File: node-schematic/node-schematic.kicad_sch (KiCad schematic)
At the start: 23 parts, among them U1 NRF52840-QFAA-R7, X1 NX2016SA-32MHZ, X2 32.768kHz

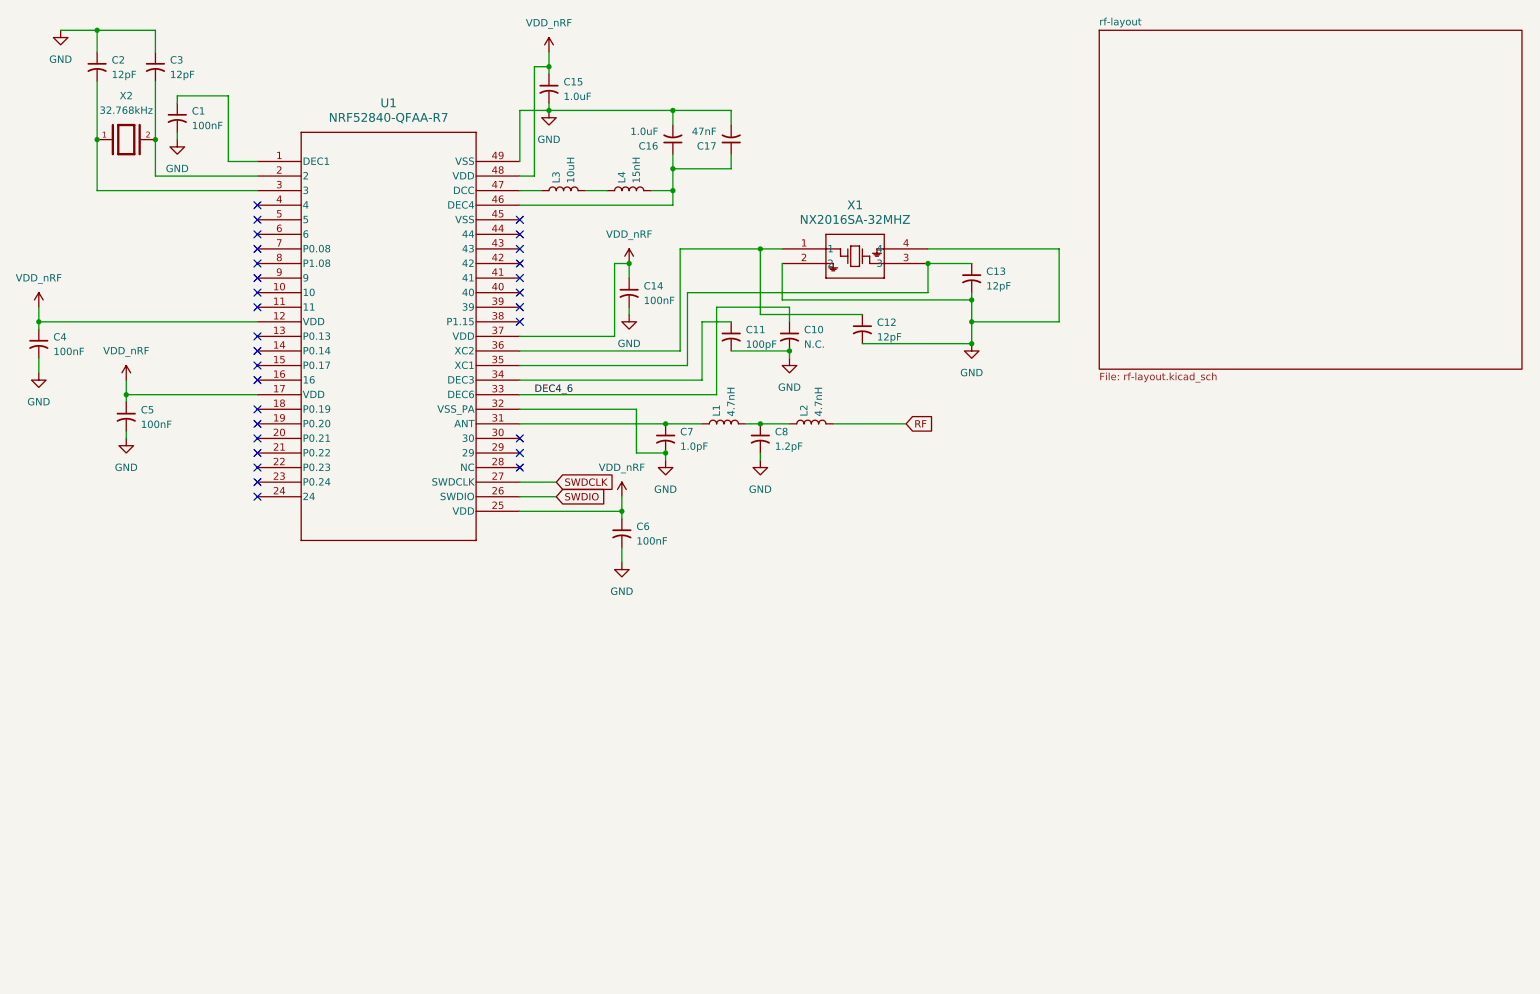
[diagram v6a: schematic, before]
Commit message: fuel gauge implemented
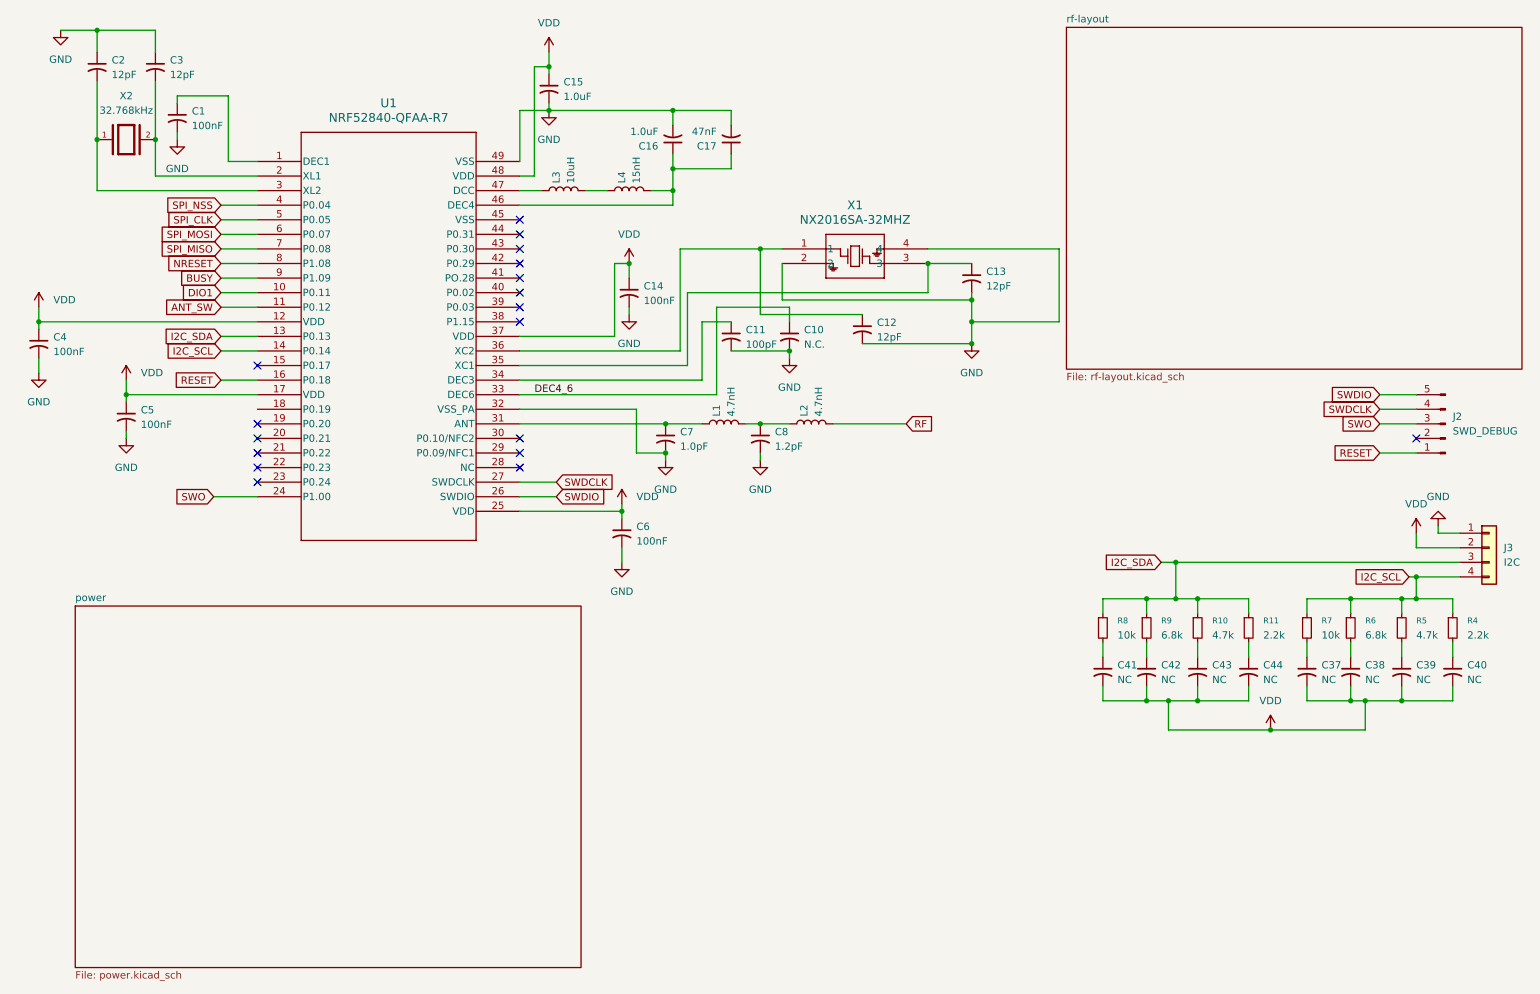
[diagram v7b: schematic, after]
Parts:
- added C37, C38, C39, C40, C41, C42, C43, C44: NC, Jumper:SolderJumper-2_P1.3mm_Open_Pad1.0x1.5mm, symbol Device:C_Small_US
- added J2: SWD_DEBUG, Connector_PinSocket_2.54mm:PinSocket_1x05_P2.54mm_Vertical, symbol Connector:Conn_01x05_Pin
- added J3: I2C, Connector_PinSocket_2.54mm:PinSocket_1x04_P2.54mm_Vertical, symbol Connector_Generic:Conn_01x04
- added R10, R5: 4.7k, Resistor_SMD:R_0201_0603Metric, symbol Device:R_Small
- added R11, R4: 2.2k, Resistor_SMD:R_0201_0603Metric, symbol Device:R_Small
- added R6, R9: 6.8k, Resistor_SMD:R_0201_0603Metric, symbol Device:R_Small
- added R7, R8: 10k, Resistor_SMD:R_0201_0603Metric, symbol Device:R_Small
- L3: footprint Capacitor_SMD:C_0603_1608Metric -> Inductor_SMD:L_0603_1608Metric
- L4: footprint Capacitor_SMD:C_0402_1005Metric -> Inductor_SMD:L_0402_1005Metric
- U1: footprint QFN48_NRF52840-QFAA-R7_NOR -> NRF52840_QFAA_R7:QFN48_NRF52840-QFAA-R7_NOR
- X1: footprint NX2016SA_NDK -> NX2016SA_32MHZ_EXS00A_CS11336:NX2016SA_NDK
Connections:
- net GND: now also J3.1 (Pin_1)
- net SWDCLK: now also J2.4 (Pin_4)
- net SWDIO: now also J2.5 (Pin_5)
- net DIO1: now reaches U1.10 (P0.11)
- net ANT_SW: now reaches U1.11 (P0.12)
- net I2C_SDA: now reaches U1.13 (P0.13)
- net I2C_SDA: now also J3.3 (Pin_3), R10.1, R11.1, R8.1, R9.1
- net I2C_SCL: now reaches U1.14 (P0.14)
- net I2C_SCL: now also J3.4 (Pin_4), R4.1, R5.1, R6.1, R7.1
- net RESET: now reaches U1.16 (P0.18)
- net RESET: now also J2.1 (Pin_1)
- net SWO: now reaches U1.24 (P1.00)
- net SWO: now also J2.3 (Pin_3)
- net SPI_NSS: now reaches U1.4 (P0.04)
- net SPI_CLK: now reaches U1.5 (P0.05)
- net SPI_MOSI: now reaches U1.6 (P0.07)
- net SPI_MISO: now reaches U1.7 (P0.08)
- net NRESET: now reaches U1.8 (P1.08)
- net BUSY: now reaches U1.9 (P1.09)
- net VDD_nRF renamed VDD
- net VDD: now also C37.2, C38.2, C39.2, C40.2, C41.2, C42.2, C43.2, C44.2, J3.2 (Pin_2)
- new net: C41.1, R8.2
- new net: C39.1, R5.2
- new net: C42.1, R9.2
- new net: C38.1, R6.2
- new net: C43.1, R10.2
- new net: C40.1, R4.2
- new net: C37.1, R7.2
- new net: C44.1, R11.2
- no-connect marks 30 -> 18
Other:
- added sheet power (power.kicad_sch)

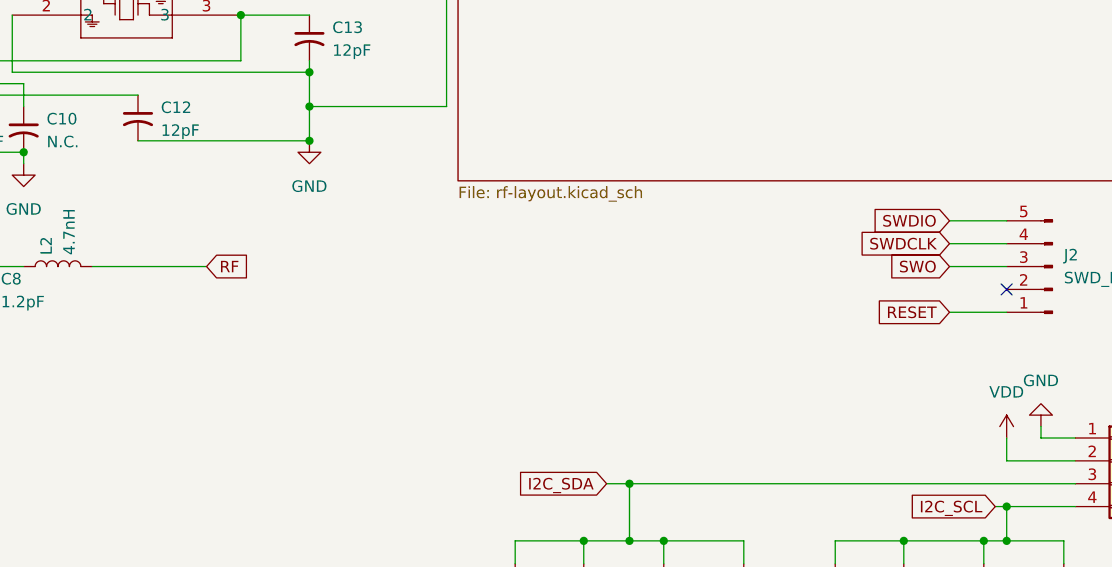
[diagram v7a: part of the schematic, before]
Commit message: completed pcb and box
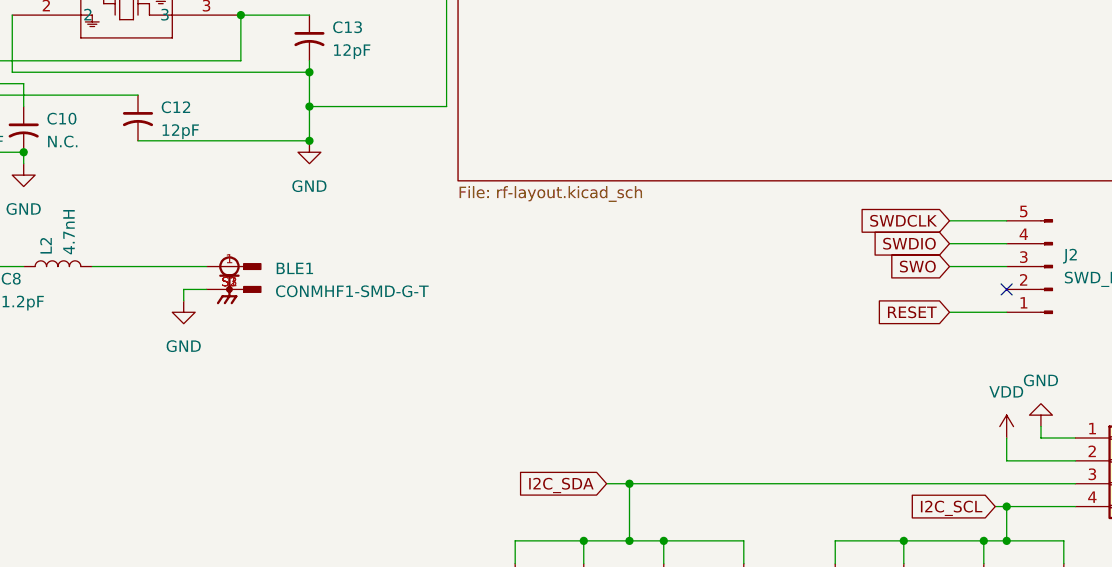
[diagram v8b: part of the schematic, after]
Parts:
- added BLE1: CONMHF1-SMD-G-T, CONMHF1_SMD_G_T:LINX_CONMHF1-SMD-G-T, symbol CONMHF1-SMD-G-T:CONMHF1-SMD-G-T
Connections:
- net GND: now also BLE1.S1, BLE1.S2, BLE1.S3
- net SWDCLK: now also J2.5 (Pin_5); no longer J2.4 (Pin_4)
- net SWDIO: now also J2.4 (Pin_4); no longer J2.5 (Pin_5)
- net RF: no longer names the net of L2.2
- net RF: now also BLE1.1
